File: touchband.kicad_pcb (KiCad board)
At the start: 2 copper layers, 158.8 x 33 mm, 36 parts, among them J1 Conn_01x01_Female, J10 Conn_01x01_Female, J11 Conn_01x01_Female, J12 Conn_01x01_Female, J13 Conn_01x01_Female, J14 Conn_01x01_Female, J15 Conn_01x01_Female, J16 Conn_01x01_Female, J17 Conn_01x01_Female, J18 Conn_01x01_Female, J19 Conn_01x01_Female, J2 Conn_01x01_Female, J20 Conn_01x01_Female, J21 Conn_01x01_Female, J22 Conn_01x01_Female, J23 Conn_01x01_Female, J24 Conn_01x01_Female, J3 Conn_01x01_Female, J4 \, J5 Conn_01x01_Female, J6 Conn_01x01_Female, J7 Conn_01x01_Female, J8 Conn_01x01_Female, J9 Conn_01x01_Female

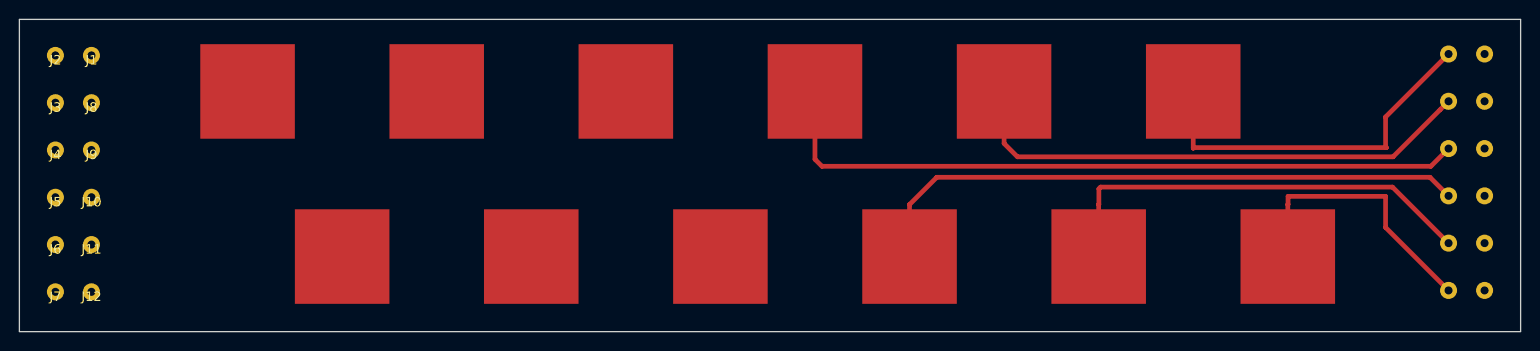
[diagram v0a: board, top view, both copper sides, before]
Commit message: finalize traces and add silk text
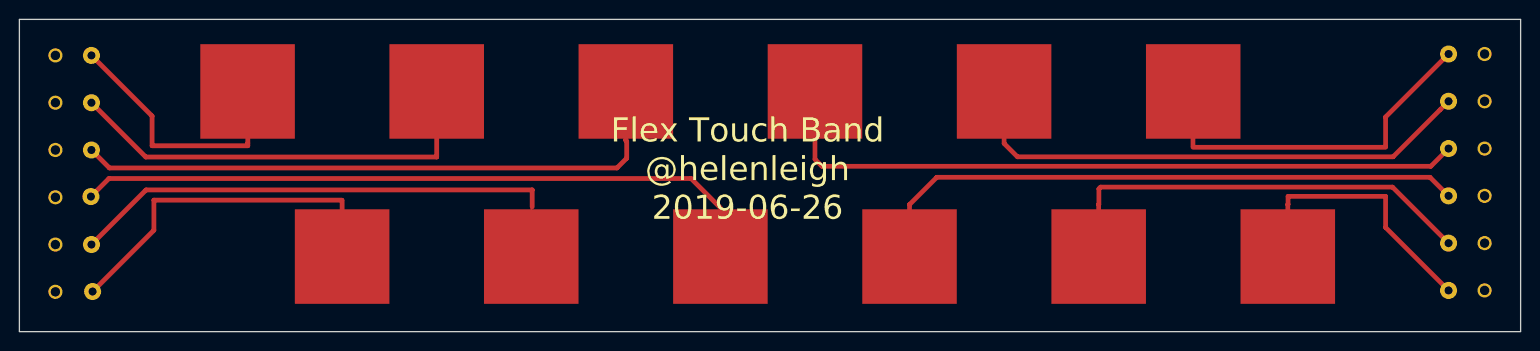
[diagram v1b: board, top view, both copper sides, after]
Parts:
- J19, J2, J20, J21, J22, J23, J24, J3, J4, J5, J6, J7: footprint touch:hole30AWG -> touch:strain30AWG
- moved J12 10.1 mm to (17.7, 28.9)
- moved J10 9.97 mm to (17.9, 38.9)
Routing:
- net Net-(J12-Pad1): track 0.00 -> 73.8 mm
- net Net-(J9-Pad1): track 0.00 -> 64.9 mm
- net Net-(J11-Pad1): track 0.00 -> 56.1 mm
- net Net-(J8-Pad1): track 0.00 -> 45.8 mm
- net Net-(J10-Pad1): track 0.00 -> 38.2 mm
- net Net-(J1-Pad1): track 0.00 -> 33.7 mm
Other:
- net class trace added: clearance 0.254, trace_width 0.508, via_dia 0.508, via_drill 0.254
- board text added: "Flex Touch Band @helenleigh 2019-06-26"
